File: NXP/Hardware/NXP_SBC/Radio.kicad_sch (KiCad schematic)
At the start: 1 part, among them U8 MAYA-W276-00B

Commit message: More additions to schematic
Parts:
- added C68, C71: 2u2F, Capacitor_SMD:C_0603_1608Metric_Pad1.08x0.95mm_HandSolder, symbol Device:C_Small
- added C69, C70, C72: 100nF, Capacitor_SMD:C_0603_1608Metric_Pad1.08x0.95mm_HandSolder, symbol Device:C_Small
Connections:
- net GND_10 is gone; now on net GND: U8.H5 (GND_10)
- net GND: now also U8.F5 (GND_8), U8.H4 (GND_9), U8.K2 (GND_11), U8.K3 (GND_12), U8.K4 (GND_13), U8.K6 (GND_14), U8.K7 (GND_15), U8.K8 (GND_16), U8.L1 (GND_17), U8.M1 (GND_18), U8.M2 (GND_19), U8.M8 (GND_20), U8.M9 (GND_21), C68.2, C69.1, C70.1, C71.2, C72.1
- net +1V8: now reaches U8.A2 (1V8)
- net +1V8: now also C71.1, C72.2
- net RADIO_SD_CLK: now reaches U8.A4 (SD_CLK)
- net RADIO_VIO_SD: now reaches U8.A6 (VIO_SD)
- net DCDC_3V3: now reaches U8.A7 (3V3_1)
- net DCDC_3V3: now also U8.B7 (3V3_2), C68.1, C69.2, C70.2
- net RADIO_VIO: now reaches U8.A8 (VIO)
- net RADIO_GPIO[27]: now reaches U8.B1 (GPIO[27])
- net RADIO_SD_CMD: now reaches U8.B4 (SD_CMD)
- net RADIO_WCI_SOUT: now reaches U8.B6 (WCI_SOUT)
- net RADIO__EXT_REQ/SPI_FRM: now reaches U8.C2 (_EXT_REQ/SPI_FRM)
- net RADIO_WCI_SIN: now reaches U8.C6 (WCI_SIN)
- net RADIO_RST_IND: now reaches U8.C8 (RST_IND)
- net RADIO_EXT_FREQ/SPI_INT: now reaches U8.D2 (EXT_FREQ/SPI_INT)
- net RADIO_CONFIG[0]: now reaches U8.D3 (CONFIG[0])
- net RADIO_SD_INT: now reaches U8.D7 (SD_INT)
- net RADIO_PCM_CLK: now reaches U8.D8 (PCM_CLK)
- net RADIO_EXT_STATE/SPI_CL_K: now reaches U8.E2 (EXT_STATE/SPI_CL_K)
- net RADIO_CONFIG[1]: now reaches U8.E3 (CONFIG[1])
- net RADIO_BT_15.4_WAKE__HOST: now reaches U8.E7 (BT_15.4_WAKE__HOST)
- net RADIO_PCM_MCLK: now reaches U8.E8 (PCM_MCLK)
- net RADIO_PCM_DIN: now reaches U8.E9 (PCM_DIN)
- net RADIO_EXT_PRI/SPI_TX: now reaches U8.F2 (EXT_PRI/SPI_TX)
- net RADIO_RF_CNTL3: now reaches U8.F3 (RF_CNTL3)
- net RADIO_RF_ANT1: now reaches U8.K9 (RF_ANT1)
- net RADIO_ANT_FEED: now reaches U8.L9 (ANT_FEED)
- net BT_15.4_DEV_WAK_E renamed RADIO_BT_15.4_DEV_WAK_E
- net BT_15.4_RST renamed RADIO_BT_15.4_RST
- net EXT_GNT/SPI_RX renamed RADIO_EXT_GNT/SPI_RX
- net JTAG_TCK renamed RADIO_JTAG_TCK
- net JTAG_TDI renamed RADIO_JTAG_TDI
- net JTAG_TDO renamed RADIO_JTAG_TDO
- net JTAG_TMS renamed RADIO_JTAG_TMS
- net PCM_DOUT renamed RADIO_PCM_DOUT
- net PCM_SYNC renamed RADIO_PCM_SYNC
- net PDN renamed RADIO_PDN
- net RF_ANT0 renamed RADIO_RF_ANT0
- net RF_CNTL0 renamed RADIO_RF_CNTL0
- net RF_CNTL2 renamed RADIO_RF_CNTL2
- net RF_CNTL4 renamed RADIO_RF_CNTL4
- net SD_DAT[0] renamed RADIO_SD_DAT[0]
- net SD_DAT[1] renamed RADIO_SD_DAT[1]
- net SD_DAT[2] renamed RADIO_SD_DAT[2]
- net SD_DAT[3] renamed RADIO_SD_DAT[3]
- net UART_CTS renamed RADIO_UART_CTS
- net UART_RTS renamed RADIO_UART_RTS
- net UART_RX renamed RADIO_UART_RX
- net UART_TX renamed RADIO_UART_TX
- net WL_DEV_WAKE renamed RADIO_WL_DEV_WAKE
- net WL_RST renamed RADIO_WL_RST
- net WL_WAKE_HOST renamed RADIO_WL_WAKE_HOST
- no-connect marks 5 -> 15

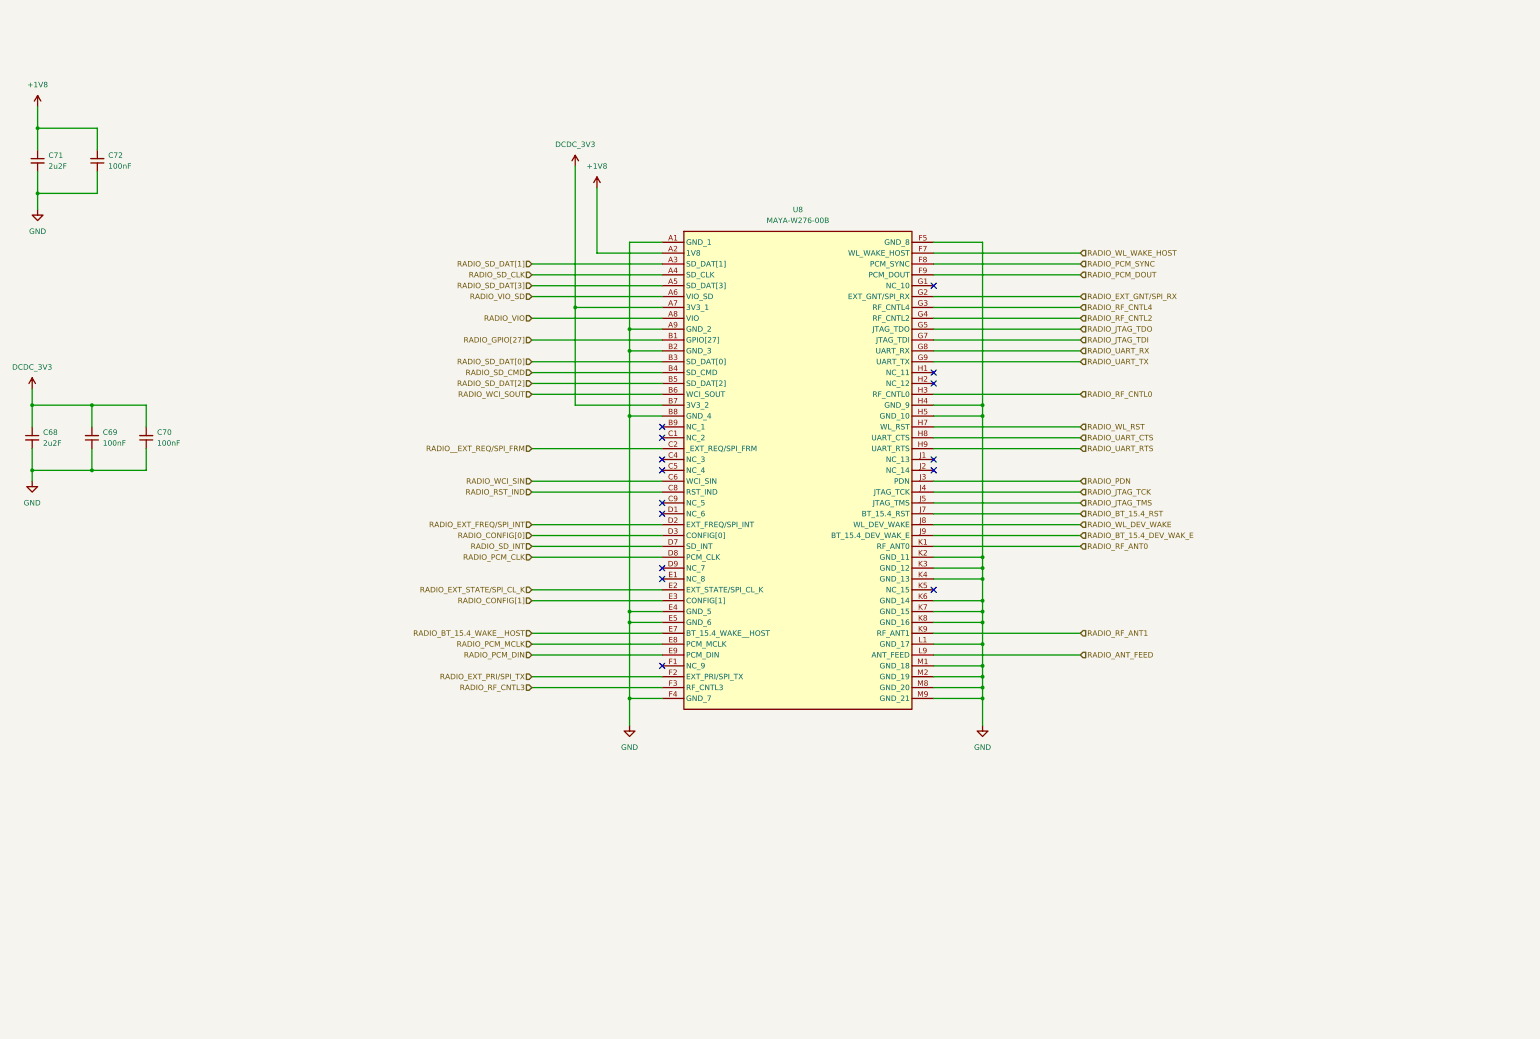
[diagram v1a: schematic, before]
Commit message: Updates to radio connections
Also used the pin configurator tool to better understand pin mapping of the imx processor
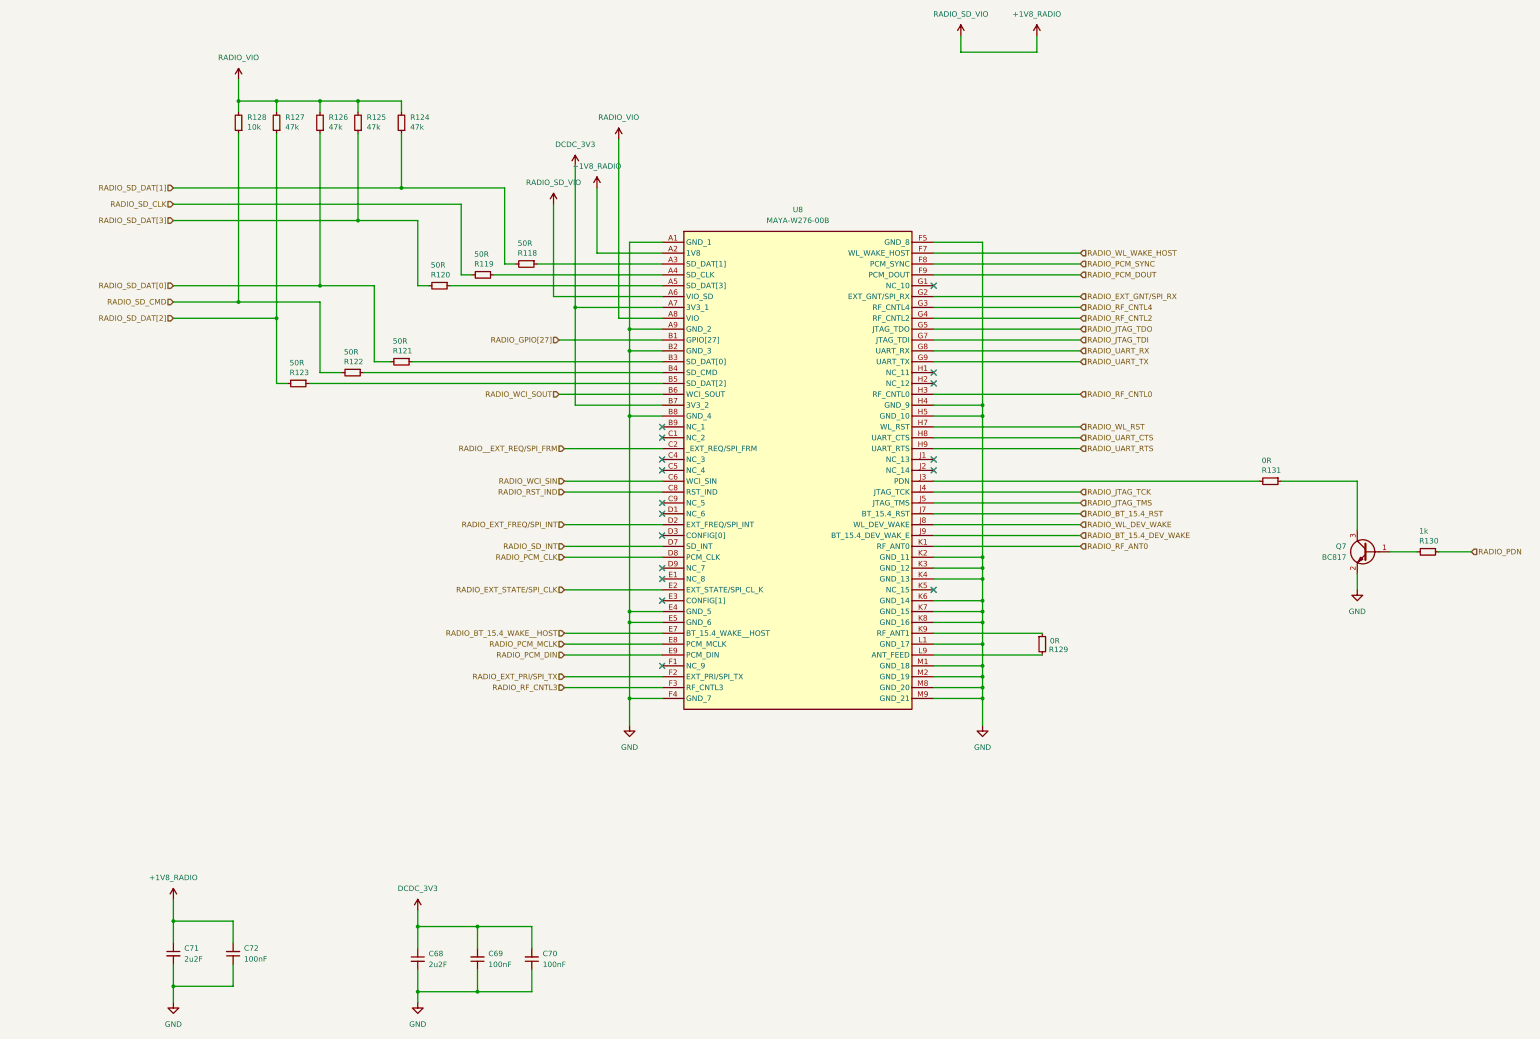
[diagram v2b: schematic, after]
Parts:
- added Q7: BC817, Package_TO_SOT_SMD:SOT-23, symbol Transistor_BJT:BC817
- added R118, R119, R120, R121, R122, R123: 50R, Resistor_SMD:R_01005_0402Metric, symbol Device:R_Small
- added R124, R125, R126, R127: 47k, Resistor_SMD:R_01005_0402Metric, symbol Device:R_Small
- added R128: 10k, Resistor_SMD:R_01005_0402Metric, symbol Device:R_Small
- added R129, R131: 0R, Resistor_SMD:R_01005_0402Metric, symbol Device:R_Small
- added R130: 1k, Resistor_SMD:R_01005_0402Metric, symbol Device:R_Small
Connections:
- net RADIO_VIO_SD is gone; now on net +1V8_RADIO: U8.A6 (VIO_SD)
- net GND: now also Q7.2 (E)
- net RADIO_PDN: now also R130.1; no longer U8.J3 (PDN)
- net RADIO_SD_CLK: now also R119.2; no longer U8.A4 (SD_CLK)
- net RADIO_SD_CMD: now also R122.2, R128.1; no longer U8.B4 (SD_CMD)
- net RADIO_SD_DAT[0]: now also R121.2, R126.1; no longer U8.B3 (SD_DAT[0])
- net RADIO_SD_DAT[1]: now also R118.2, R124.1; no longer U8.A3 (SD_DAT[1])
- net RADIO_SD_DAT[2]: now also R123.2, R127.1; no longer U8.B5 (SD_DAT[2])
- net RADIO_SD_DAT[3]: now also R120.2, R125.1; no longer U8.A5 (SD_DAT[3])
- net RADIO_VIO: now also R124.2, R125.2, R126.2, R127.2, R128.2
- net +1V8 renamed +1V8_RADIO
- net RADIO_ANT_FEED: no longer names the net of U8.L9 (ANT_FEED)
- net RADIO_ANT_FEED: now also R129.2
- net RADIO_BT_15.4_DEV_WAK_E renamed RADIO_BT_15.4_DEV_WAKE
- net RADIO_CONFIG[0]: no longer names the net of U8.D3 (CONFIG[0])
- net RADIO_CONFIG[1]: no longer names the net of U8.E3 (CONFIG[1])
- net RADIO_EXT_STATE/SPI_CL_K renamed RADIO_EXT_STATE/SPI_CLK
- net RADIO_RF_ANT1: no longer names the net of U8.K9 (RF_ANT1)
- net RADIO_RF_ANT1: now also R129.1
- new net: R118.1, U8.A3 (SD_DAT[1])
- new net: Q7.1 (B), R130.2
- new net: Q7.3 (C), R131.1
- new net: R131.2, U8.J3 (PDN)
- new net: R123.1, U8.B5 (SD_DAT[2])
- new net: R119.1, U8.A4 (SD_CLK)
- new net: R121.1, U8.B3 (SD_DAT[0])
- new net: R120.1, U8.A5 (SD_DAT[3])
- new net: R122.1, U8.B4 (SD_CMD)
- no-connect marks 15 -> 17
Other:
- moved on the sheet: C68, C69, C70, C71, C72

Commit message: minor updates
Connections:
- net RADIO_EXT_STATE/SPI_CLK renamed RADIO_EXT_STATE/SPI_CLK

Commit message: minor updates
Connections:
- net RADIO_VIO is gone; now on net DCDC_3V3: R124.2, R125.2, R126.2, R127.2, R128.2, U8.A8 (VIO)
- net +1V8_RADIO: no longer U8.A6 (VIO_SD)
- net DCDC_3V3: now also U8.A6 (VIO_SD)
